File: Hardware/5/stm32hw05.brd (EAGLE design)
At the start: 54 x 55 mm, 46 parts

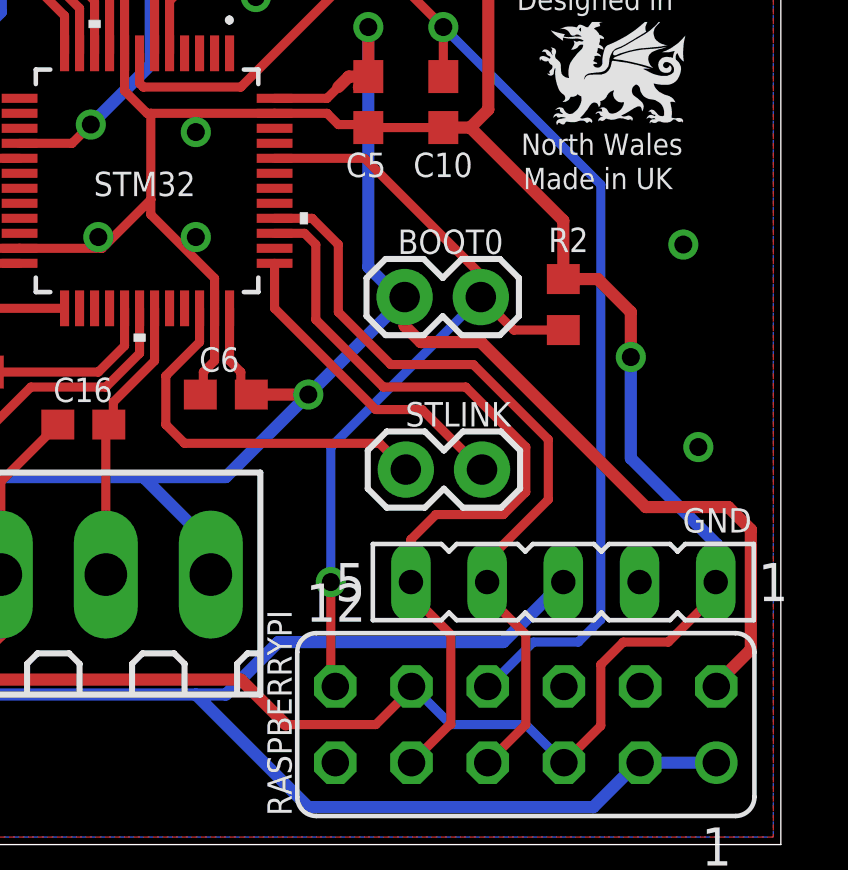
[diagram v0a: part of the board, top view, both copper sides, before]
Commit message: added NRST & 3.3v routing
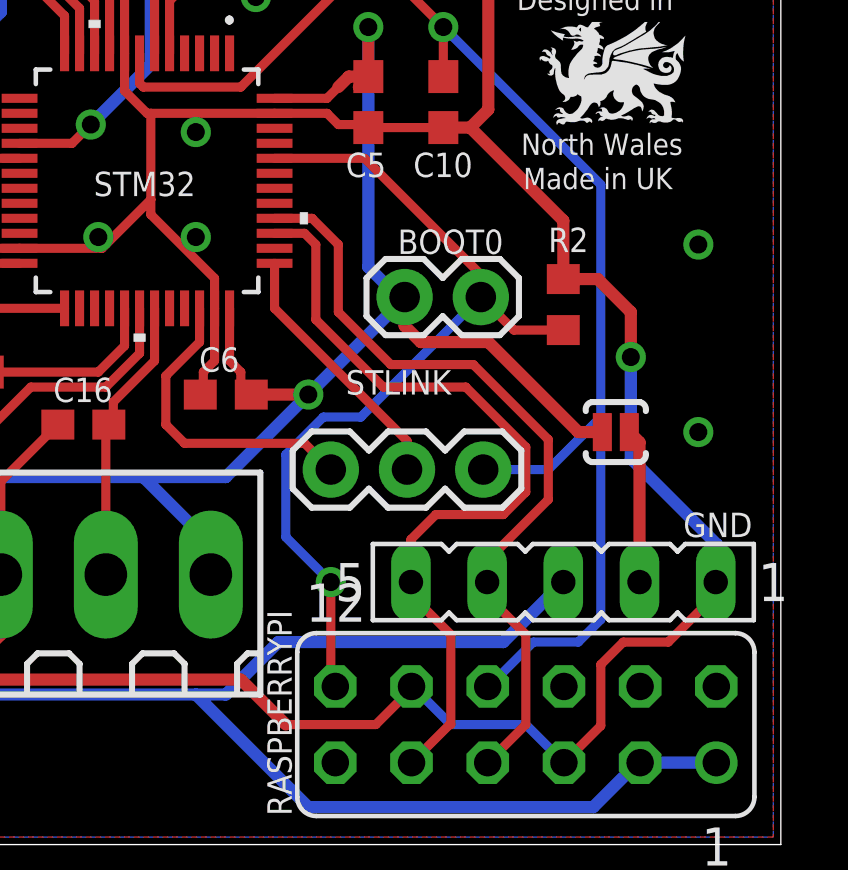
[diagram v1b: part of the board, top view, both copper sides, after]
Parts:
- added SJ1: SOLDERJUMPERNO, SparkFun:SJ_2S-NO
- STLINK: device SparkFun:1X02 -> SparkFun:1X03
- moved STLINK 2.50 mm to (39.0, 12.5)
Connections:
- new net N$1: GND.2, SJ1.1
- net +3V3: now also SJ1.2
- net NRST: now also STLINK.3
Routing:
- net +3V3: track 139.2 -> 127.3 mm
- net N$1: track 0.00 -> 5.14 mm
- net NRST: track 41.4 -> 46.1 mm
- net SWDIO: track 13.0 -> 10.5 mm
- net BOOT0: track 27.5 -> 29.5 mm
- net SWCLK: track 10.6 -> 8.70 mm
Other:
- board text added: "3.3"
- board text added: "5V"
- board text added: "RST"
- board text added: "RX"
- board text added: "TX"
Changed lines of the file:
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@@
 <wire x1="54" y1="55" x2="0" y2="55" width="0" layer="20"/>
 <wire x1="0" y1="55" x2="0" y2="0" width="0" layer="20"/>
-<text x="38" y="12" size="0.8128" layer="27" font="vector" ratio="20">DIO</text>
-<text x="45.5" y="12" size="0.8128" layer="27" font="vector" ratio="20">CLK</text>
+<text x="38" y="14" size="0.8128" layer="27" font="vector" ratio="20">DIO</text>
+<text x="40.5" y="14" size="0.8128" layer="27" font="vector" ratio="20">CLK</text>
 <text x="16.375" y="3.875" size="0.8128" layer="27" font="vector" ratio="20">GND</text>
 <text x="20.75" y="3.75" size="0.8128" layer="27" font="vector" ratio="20">T</text>
@@
 <rectangle x1="49.461440625" y1="27.413721875" x2="49.556640625" y2="27.420121875" layer="21"/>
 <rectangle x1="49.924940625" y1="27.413721875" x2="49.969440625" y2="27.420121875" layer="21"/>
+<text x="48.5" y="10.25" size="0.8128" layer="27" font="vector" ratio="20">3.3</text>
+<text x="46" y="10.25" size="0.8128" layer="27" font="vector" ratio="20">5V</text>
+<text x="43.25" y="14" size="0.8128" layer="27" font="vector" ratio="20">RST</text>
+<text x="43.5" y="10.25" size="0.8128" layer="27" font="vector" ratio="20">RX</text>
+<text x="41" y="10.25" size="0.8128" layer="27" font="vector" ratio="20">TX</text>
 </plain>
 <attributes>
@@
 </element>
 <element name="GND" library="con-lsta" package="FE05-1" value="UART" x="46.75" y="8.75" smashed="yes" rot="R180">
-<attribute name="NAME" x="50.73" y="10.401" size="0.8128" layer="25" font="vector" ratio="20"/>
-<attribute name="VALUE" x="45.48" y="10.329" size="0.8128" layer="27" font="vector" ratio="20"/>
+<attribute name="NAME" x="50.75" y="10.25" size="0.8128" layer="25" font="vector" ratio="20"/>
+<attribute name="VALUE" x="49.75" y="11.25" size="0.8128" layer="27" font="vector" ratio="20"/>
 <attribute name="OC_NEWARK" value="unknown" x="46.75" y="8.75" size="1.778" layer="27" rot="R180" display="off"/>
 <attribute name="MPN" value="" x="46.75" y="8.75" size="1.778" layer="27" rot="R180" display="off"/>
@@
 <attribute name="VALUE" x="33.25" y="29.75" size="0.8128" layer="27" font="vector" ratio="20"/>
 </element>
-<element name="STLINK" library="SparkFun" package="1X02" value="" x="41.5" y="12.5" smashed="yes">
-<attribute name="NAME" x="45" y="14.75" size="0.8128" layer="25" font="vector" ratio="20" rot="R180"/>
-<attribute name="VALUE" x="40.23" y="9.325" size="1.27" layer="27"/>
+<element name="STLINK" library="SparkFun" package="1X03" value="" x="39" y="12.5" smashed="yes">
+<attribute name="NAME" x="39.5" y="15" size="0.8128" layer="25" font="vector" ratio="20"/>
+<attribute name="VALUE" x="37.73" y="9.325" size="1.27" layer="27"/>
 </element>
 <element name="C16" library="resistor" package="C0603" value="100nF" x="30.75" y="14" smashed="yes">
@@
 <element name="LOGO1" library="ohw-logo" package="OSHW_6X200_NOTEXT" value="OSHW_LOGO_6MILX0200-NT" x="5.79" y="4.091" smashed="yes"/>
 <element name="U$1" library="adafruit" package="DCJACK_2MM_SMT" value="2.1MMJACKSMT" x="9" y="52.25" rot="R270"/>
+<element name="SJ1" library="SparkFun" package="SJ_2S-NO" value="SOLDERJUMPERNO" x="48.5" y="13.75" smashed="yes" rot="R180"/>
 </elements>
 <signals>
@@
 <via x="36.5" y="28.25" extent="1-16" drill="0.6"/>
 <via x="14.25" y="17.5" extent="1-16" drill="0.6"/>
-<via x="50.75" y="20" extent="1-16" drill="0.6"/>
+<via x="51.25" y="20" extent="1-16" drill="0.6"/>
 <via x="16.25" y="37.25" extent="1-16" drill="0.6"/>
 <via x="16.25" y="45.25" extent="1-16" drill="0.6"/>
@@
 <via x="31.25" y="20.25" extent="1-16" drill="0.6"/>
 <via x="3" y="32.25" extent="1-16" drill="0.6"/>
-<via x="51.25" y="13.25" extent="1-16" drill="0.6"/>
+<via x="51.25" y="13.75" extent="1-16" drill="0.6"/>
 </signal>
 <signal name="+5V">
@@
 <wire x1="26.75" y1="19" x2="25.85" y2="19" width="0.3048" layer="1"/>
 <wire x1="25.85" y1="19" x2="25.75" y2="18.9" width="0.3048" layer="1"/>
-<wire x1="52.25" y1="11.25" x2="49.5" y2="11.25" width="0.4064" layer="1"/>
-<wire x1="49.5" y1="11.25" x2="44" y2="16.75" width="0.4064" layer="1"/>
-<wire x1="44" y1="16.75" x2="42" y2="16.75" width="0.4064" layer="1"/>
+<wire x1="44.25" y1="16.75" x2="42" y2="16.75" width="0.4064" layer="1"/>
 <wire x1="42" y1="16.75" x2="41.46" y2="17.29" width="0.4064" layer="1"/>
 <contactref element="DS18B20" pad="3"/>
@@
 <wire x1="38.25" y1="15" x2="41.46" y2="18.21" width="0.4064" layer="16"/>
 <wire x1="41.46" y1="18.21" x2="41.46" y2="18.25" width="0.4064" layer="16"/>
-<wire x1="51.85" y1="5.35" x2="53" y2="6.5" width="0.4064" layer="1"/>
-<wire x1="53" y1="6.5" x2="53" y2="10.5" width="0.4064" layer="1"/>
-<wire x1="53" y1="10.5" x2="52.25" y2="11.25" width="0.4064" layer="1"/>
+<contactref element="SJ1" pad="2"/>
+<wire x1="44.25" y1="16.75" x2="47.25" y2="13.75" width="0.4064" layer="1"/>
+<wire x1="47.25" y1="13.75" x2="48.05" y2="13.75" width="0.4064" layer="1"/>
 </signal>
 <signal name="BOOT0">
@@
 <wire x1="44" y1="18.25" x2="45.1" y2="17.15" width="0.3048" layer="1"/>
 <wire x1="45.1" y1="17.15" x2="46.75" y2="17.15" width="0.3048" layer="1"/>
-<wire x1="39" y1="13.25" x2="44" y2="18.25" width="0.3048" layer="16"/>
-<wire x1="39" y1="13.25" x2="39" y2="8.75" width="0.3048" layer="16"/>
 <via x="39" y="8.75" extent="1-16" drill="0.6"/>
 <wire x1="39" y1="8.75" x2="39" y2="5.42" width="0.3048" layer="1"/>
 <wire x1="39" y1="5.42" x2="39.15" y2="5.27" width="0.3048" layer="1"/>
+<wire x1="44" y1="18.25" x2="40" y2="14.25" width="0.3048" layer="16"/>
+<wire x1="40" y1="14.25" x2="38.75" y2="14.25" width="0.3048" layer="16"/>
+<wire x1="38.75" y1="14.25" x2="37.5" y2="13" width="0.3048" layer="16"/>
+<wire x1="37.5" y1="13" x2="37.5" y2="10.25" width="0.3048" layer="16"/>
+<wire x1="37.5" y1="10.25" x2="39" y2="8.75" width="0.3048" layer="16"/>
 </signal>
 <signal name="VBAT">
@@
 <wire x1="42.75" y1="25.6" x2="42.75" y2="27.25" width="0.3048" layer="1"/>
 <wire x1="42.75" y1="27.25" x2="48" y2="22" width="0.3048" layer="16"/>
-<wire x1="48" y1="22" x2="48" y2="7.5" width="0.3048" layer="16"/>
+<wire x1="48" y1="22" x2="48" y2="14.25" width="0.3048" layer="16"/>
 <via x="42.75" y="27.25" extent="1-16" drill="0.6"/>
+<contactref element="STLINK" pad="3"/>
+<wire x1="48" y1="14.25" x2="48" y2="7.5" width="0.3048" layer="16"/>
+<wire x1="44.08" y1="12.5" x2="46.25" y2="12.5" width="0.3048" layer="16"/>
+<wire x1="46.25" y1="12.5" x2="48" y2="14.25" width="0.3048" layer="16"/>
 </signal>
 <signal name="SWDIO">
 <contactref element="STLINK" pad="1"/>
 <contactref element="STM32" pad="34"/>
-<wire x1="41.5" y1="12.5" x2="40.625" y2="13.375" width="0.3048" layer="1"/>
-<wire x1="40.625" y1="13.375" x2="34.125" y2="13.375" width="0.3048" layer="1"/>
 <wire x1="34.125" y1="13.375" x2="33.5" y2="14" width="0.3048" layer="1"/>
 <wire x1="33.5" y1="14" x2="33.5" y2="15.625" width="0.3048" layer="1"/>
 <wire x1="33.5" y1="15.625" x2="34.625" y2="16.75" width="0.3048" layer="1"/>
 <wire x1="34.625" y1="16.75" x2="34.625" y2="17.875" width="0.3048" layer="1"/>
+<wire x1="34.125" y1="13.375" x2="38.125" y2="13.375" width="0.3048" layer="1"/>
+<wire x1="38.125" y1="13.375" x2="39" y2="12.5" width="0.3048" layer="1"/>
 </signal>
 <signal name="SWCLK">
 <contactref element="STLINK" pad="2"/>
 <contactref element="STM32" pad="37"/>
-<wire x1="44.04" y1="12.5" x2="42.04" y2="14.5" width="0.3048" layer="1"/>
-<wire x1="42.04" y1="14.5" x2="40.5" y2="14.5" width="0.3048" layer="1"/>
-<wire x1="40.5" y1="14.5" x2="37.125" y2="17.875" width="0.3048" layer="1"/>
+<wire x1="41.54" y1="13.46" x2="37.125" y2="17.875" width="0.3048" layer="1"/>
 <wire x1="37.125" y1="17.875" x2="37.125" y2="19.375" width="0.3048" layer="1"/>
+<wire x1="41.54" y1="13.46" x2="41.54" y2="12.5" width="0.3048" layer="1"/>
 </signal>
 <signal name="BIAS">
@@
 <signal name="N$3">
 </signal>
+<signal name="N$1">
+<contactref element="GND" pad="2"/>
+<contactref element="SJ1" pad="1"/>
+<wire x1="49.29" y1="8.75" x2="49.29" y2="13.41" width="0.4064" layer="1"/>
+<wire x1="49.29" y1="13.41" x2="48.95" y2="13.75" width="0.4064" layer="1"/>
+</signal>
 </signals>

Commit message: move UART to PA9 & PA10, move pulse, LED & ds18b20
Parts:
- moved C16 0.50 mm to (30.2, 14.0)
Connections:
- net DS18B20: now also STM32.21; no longer STM32.30
- net LED: now also STM32.27; no longer STM32.29
- net PULSE: now also STM32.28; no longer STM32.31
- net UART_RX: now also STM32.31; no longer STM32.40
- net UART_TX: now also STM32.30; no longer STM32.39
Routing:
- net UART_TX: track 27.3 -> 23.2 mm
- net UART_RX: track 26.2 -> 25.3 mm
- net LED: track 6.14 -> 5.28 mm
- net DS18B20: track 20.4 -> 20.7 mm, vias 0 -> 2
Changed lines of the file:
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@@
 <setting verticaltext="up"/>
 </settings>
-<grid distance="9.84251969" unitdist="mil" unit="mil" style="lines" multiple="1" display="yes" altdistance="0.025" altunitdist="inch" altunit="inch"/>
+<grid distance="0.125" unitdist="mm" unit="mm" style="lines" multiple="1" display="yes" altdistance="0.025" altunitdist="inch" altunit="inch"/>
 <layers>
 <layer number="1" name="Top" color="4" fill="1" visible="yes" active="yes"/>
@@
 <attribute name="VALUE" x="37.73" y="9.325" size="1.27" layer="27"/>
 </element>
-<element name="C16" library="resistor" package="C0603" value="100nF" x="30.75" y="14" smashed="yes">
-<attribute name="NAME" x="29.75" y="14.75" size="0.8128" layer="25" font="vector" ratio="20"/>
+<element name="C16" library="resistor" package="C0603" value="100nF" x="30.25" y="14" smashed="yes">
+<attribute name="NAME" x="29.25" y="14.75" size="0.8128" layer="25" font="vector" ratio="20"/>
 </element>
 <element name="R1" library="resistor" package="R0603" value="4.7k" x="19.25" y="14" smashed="yes" rot="R180">
@@
 <contactref element="PULSE" pad="1"/>
 <contactref element="DS18B20" pad="1"/>
-<wire x1="28" y1="12.1" x2="29.9" y2="14" width="0.3048" layer="1"/>
 <wire x1="19.25" y1="5.5" x2="26.5" y2="5.5" width="0.4064" layer="1"/>
 <wire x1="26.5" y1="5.5" x2="36" y2="5.5" width="0.4064" layer="1"/>
@@
 <wire x1="28" y1="9" x2="28" y2="7" width="0.4064" layer="1"/>
 <wire x1="28" y1="7" x2="26.5" y2="5.5" width="0.4064" layer="1"/>
-<wire x1="28" y1="12.1" x2="28" y2="9" width="0.3048" layer="1"/>
+<wire x1="28" y1="12.6" x2="28" y2="9" width="0.3048" layer="1"/>
 <wire x1="41.69" y1="5.31" x2="41.69" y2="5.19" width="0.3048" layer="1"/>
 <wire x1="41.69" y1="5.19" x2="40.5" y2="4" width="0.3048" layer="1"/>
@@
 <via x="25.25" y="27.25" extent="1-16" drill="0.6"/>
 <via x="26.5" y="24.25" extent="1-16" drill="0.6"/>
-<via x="36.5" y="28.25" extent="1-16" drill="0.6"/>
 <via x="14.25" y="17.5" extent="1-16" drill="0.6"/>
 <via x="51.25" y="20" extent="1-16" drill="0.6"/>
@@
 <via x="3" y="32.25" extent="1-16" drill="0.6"/>
 <via x="51.25" y="13.75" extent="1-16" drill="0.6"/>
+<wire x1="28" y1="12.6" x2="29.4" y2="14" width="0.3048" layer="1"/>
+<via x="23" y="21.75" extent="1-16" drill="0.6"/>
 </signal>
 <signal name="+5V">
@@
 <signal name="DS18B20">
 <contactref element="R1" pad="1"/>
-<contactref element="STM32" pad="30"/>
 <contactref element="DS18B20" pad="2"/>
 <wire x1="21" y1="9" x2="21" y2="10.5" width="0.3048" layer="1"/>
 <wire x1="21" y1="10.5" x2="20.1" y2="11.4" width="0.3048" layer="1"/>
 <wire x1="20.1" y1="11.4" x2="20.1" y2="14" width="0.3048" layer="1"/>
-<wire x1="29" y1="15.25" x2="27.75" y2="14" width="0.3048" layer="1"/>
-<wire x1="29" y1="15.25" x2="31.5" y2="15.25" width="0.3048" layer="1"/>
-<wire x1="31.5" y1="15.25" x2="32.625" y2="16.375" width="0.3048" layer="1"/>
-<wire x1="32.625" y1="16.375" x2="32.625" y2="17.875" width="0.3048" layer="1"/>
-<wire x1="27.75" y1="14" x2="20.1" y2="14" width="0.3048" layer="1"/>
+<contactref element="STM32" pad="21"/>
+<wire x1="28.625" y1="20.875" x2="27.375" y2="20.875" width="0.3048" layer="1"/>
+<wire x1="27.375" y1="20.875" x2="27.25" y2="21" width="0.3048" layer="1"/>
+<via x="27.25" y="21" extent="1-16" drill="0.6"/>
+<wire x1="27.25" y1="21" x2="27.25" y2="14.5" width="0.3048" layer="16"/>
+<wire x1="27.25" y1="14.5" x2="26.75" y2="14" width="0.3048" layer="16"/>
+<via x="26.75" y="14" extent="1-16" drill="0.6"/>
+<wire x1="20.1" y1="14" x2="26.75" y2="14" width="0.3048" layer="1"/>
 </signal>
 <signal name="PULSE">
 <contactref element="C16" pad="2"/>
 <contactref element="PULSE" pad="2"/>
-<contactref element="STM32" pad="31"/>
-<wire x1="31.5" y1="9" x2="31.5" y2="13.9" width="0.3048" layer="1"/>
-<wire x1="31.5" y1="13.9" x2="31.6" y2="14" width="0.3048" layer="1"/>
-<wire x1="31.6" y1="14" x2="31.75" y2="14" width="0.3048" layer="1"/>
-<wire x1="31.75" y1="14" x2="31.75" y2="14.75" width="0.3048" layer="1"/>
-<wire x1="31.75" y1="14.75" x2="33.125" y2="16.125" width="0.3048" layer="1"/>
-<wire x1="33.125" y1="16.125" x2="33.125" y2="17.875" width="0.3048" layer="1"/>
+<wire x1="31.5" y1="13.9" x2="31.1" y2="14" width="0.3048" layer="1"/>
+<contactref element="STM32" pad="28"/>
+<wire x1="31.5" y1="9" x2="31.5" y2="13.6" width="0.3048" layer="1"/>
+<wire x1="31.5" y1="13.6" x2="31.1" y2="14" width="0.3048" layer="1"/>
+<wire x1="31.1" y1="14" x2="31.625" y2="14.525" width="0.3048" layer="1"/>
+<wire x1="31.625" y1="14.525" x2="31.625" y2="17.875" width="0.3048" layer="1"/>
 </signal>
 <signal name="LSE_IN">
@@
 <signal name="LED">
 <contactref element="R3" pad="2"/>
-<contactref element="STM32" pad="29"/>
-<wire x1="27.6" y1="15.75" x2="31.25" y2="15.75" width="0.3048" layer="1"/>
-<wire x1="32.125" y1="16.625" x2="32.125" y2="17.875" width="0.3048" layer="1"/>
-<wire x1="31.25" y1="15.75" x2="32.125" y2="16.625" width="0.3048" layer="1"/>
+<contactref element="STM32" pad="27"/>
+<wire x1="31.125" y1="17.875" x2="31.125" y2="16.375" width="0.3048" layer="1"/>
+<wire x1="31.125" y1="16.375" x2="30.5" y2="15.75" width="0.3048" layer="1"/>
+<wire x1="30.5" y1="15.75" x2="27.6" y2="15.75" width="0.3048" layer="1"/>
 </signal>
 <signal name="UART_RX">
-<contactref element="STM32" pad="40"/>
 <contactref element="GND" pad="4"/>
 <contactref element="RASPBERRYPI" pad="7"/>
@@
 <wire x1="44.21" y1="8.75" x2="44.25" y2="8.79" width="0.3048" layer="1"/>
 <wire x1="44.25" y1="8.79" x2="44.25" y2="9.5" width="0.3048" layer="1"/>
-<wire x1="37.125" y1="20.875" x2="38.375" y2="20.875" width="0.3048" layer="1"/>
-<wire x1="38.375" y1="20.875" x2="39.25" y2="20" width="0.3048" layer="1"/>
-<wire x1="39.25" y1="20" x2="39.25" y2="17.75" width="0.3048" layer="1"/>
-<wire x1="39.25" y1="17.75" x2="41" y2="16" width="0.3048" layer="1"/>
-<wire x1="41" y1="16" x2="43.75" y2="16" width="0.3048" layer="1"/>
-<wire x1="43.75" y1="16" x2="46.25" y2="13.5" width="0.3048" layer="1"/>
-<wire x1="46.25" y1="13.5" x2="46.25" y2="11.5" width="0.3048" layer="1"/>
-<wire x1="46.25" y1="11.5" x2="44.25" y2="9.5" width="0.3048" layer="1"/>
+<contactref element="STM32" pad="31"/>
+<wire x1="44.25" y1="9.5" x2="43.25" y2="10.5" width="0.3048" layer="1"/>
+<wire x1="43.25" y1="10.5" x2="38.25" y2="10.5" width="0.3048" layer="1"/>
+<wire x1="38.25" y1="10.5" x2="36.25" y2="12.5" width="0.3048" layer="1"/>
+<wire x1="36.25" y1="12.5" x2="34" y2="12.5" width="0.3048" layer="1"/>
+<wire x1="34" y1="12.5" x2="32.875" y2="13.625" width="0.3048" layer="1"/>
+<wire x1="32.875" y1="13.625" x2="32.875" y2="16" width="0.3048" layer="1"/>
+<wire x1="32.875" y1="16" x2="33.125" y2="16.25" width="0.3048" layer="1"/>
+<wire x1="33.125" y1="16.25" x2="33.125" y2="17.875" width="0.3048" layer="1"/>
 </signal>
 <signal name="UART_TX">
-<contactref element="STM32" pad="39"/>
 <contactref element="GND" pad="5"/>
 <contactref element="RASPBERRYPI" pad="9"/>
@@
 <wire x1="43" y1="7" x2="41.67" y2="8.33" width="0.3048" layer="1"/>
 <wire x1="41.67" y1="8.33" x2="41.67" y2="8.75" width="0.3048" layer="1"/>
-<wire x1="41.67" y1="8.75" x2="41.67" y2="10.17" width="0.3048" layer="1"/>
-<wire x1="41.67" y1="10.17" x2="42.5" y2="11" width="0.3048" layer="1"/>
-<wire x1="42.5" y1="11" x2="44.75" y2="11" width="0.3048" layer="1"/>
-<wire x1="44.75" y1="11" x2="45.5" y2="11.75" width="0.3048" layer="1"/>
-<wire x1="45.5" y1="11.75" x2="45.5" y2="13.25" width="0.3048" layer="1"/>
-<wire x1="45.5" y1="13.25" x2="43.5" y2="15.25" width="0.3048" layer="1"/>
-<wire x1="43.5" y1="15.25" x2="40.75" y2="15.25" width="0.3048" layer="1"/>
-<wire x1="40.75" y1="15.25" x2="38.5" y2="17.5" width="0.3048" layer="1"/>
-<wire x1="38.5" y1="17.5" x2="38.5" y2="20" width="0.3048" layer="1"/>
-<wire x1="38.5" y1="20" x2="38.125" y2="20.375" width="0.3048" layer="1"/>
-<wire x1="38.125" y1="20.375" x2="37.125" y2="20.375" width="0.3048" layer="1"/>
+<contactref element="STM32" pad="30"/>
+<wire x1="41.67" y1="8.75" x2="40.67" y2="9.75" width="0.3048" layer="1"/>
+<wire x1="40.67" y1="9.75" x2="38" y2="9.75" width="0.3048" layer="1"/>
+<wire x1="38" y1="9.75" x2="36" y2="11.75" width="0.3048" layer="1"/>
+<wire x1="36" y1="11.75" x2="33.75" y2="11.75" width="0.3048" layer="1"/>
+<wire x1="33.75" y1="11.75" x2="32.25" y2="13.25" width="0.3048" layer="1"/>
+<wire x1="32.25" y1="13.25" x2="32.25" y2="16.25" width="0.3048" layer="1"/>
+<wire x1="32.25" y1="16.25" x2="32.625" y2="16.625" width="0.3048" layer="1"/>
+<wire x1="32.625" y1="16.625" x2="32.625" y2="17.875" width="0.3048" layer="1"/>
 </signal>
 <signal name="N$3">
